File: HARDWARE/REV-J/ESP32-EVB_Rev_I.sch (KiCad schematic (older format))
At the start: 160 parts, among them CON1 TB3 DG306-5.0-3P, CON2 TB3 DG306-5.0-3P, Q1 BC817-40(SOT23), Q2 BC817-40(SOT23), Q3 Q12MHz/20pF/30ppm/2P/HC-49SM(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, Q4 BC817-40(SOT23), Q5 BC817-40(SOT23), Q6 BC817, Q7 BC817-40(SOT23), U1 BL4054B-42TPRN(SOT23-5), U10 BAT54C(SOT23-3), U2 SY8089AAAC(SOT23-5), U3 ESP-WROOM-32, U4 LAN8710A-EZC(QFN32), U5 CH340T(SSOP20W), U6 MCP2562-E/SN(SOIC-8_150mil), U7 RPM7236-H8, U8 NCP303LSN27T1G(SOT-23-5), U9 BAT54C(SOT23-3)

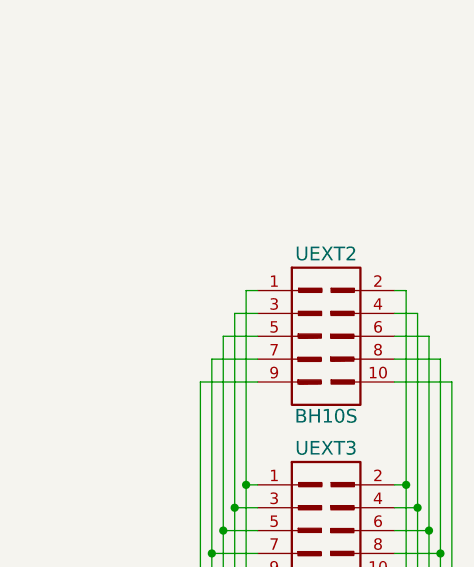
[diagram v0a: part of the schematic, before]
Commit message: fix UEXT extention
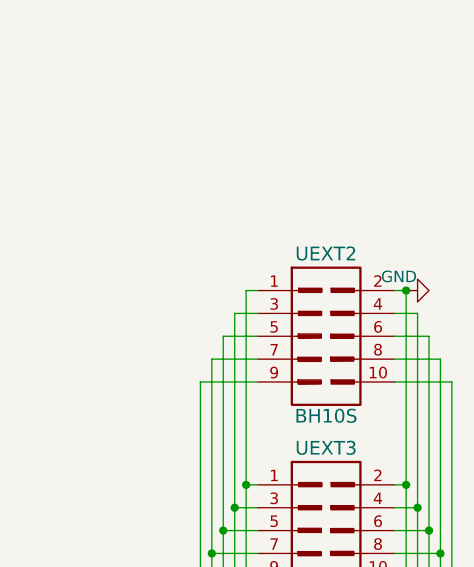
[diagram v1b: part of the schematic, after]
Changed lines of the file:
@@
 Wire Wire Line
 	23900 3950 23900 4750
+$Comp
+L ESP32-EVB_Rev_I:GND #PWR0118
+U 1 1 6378C996
+P 24800 2700
+F 0 "#PWR0118" H 24800 2450 50  0001 C CNN
+F 1 "GND" V 24860 2810 50  0000 R CNN
+F 2 "" H 24800 2700 60  0000 C CNN
+F 3 "" H 24800 2700 60  0000 C CNN
+	1    24800 2700
+	0    -1   -1   0
+$EndComp
+Connection ~ 24800 2700
 $EndSCHEMATC

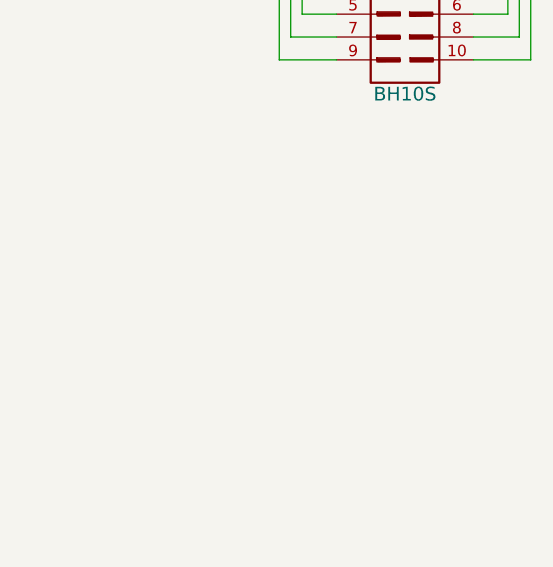
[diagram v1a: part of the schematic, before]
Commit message: add hole mount splitter
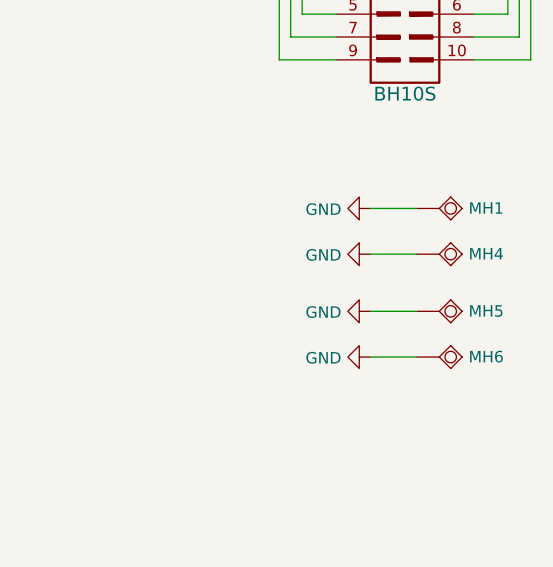
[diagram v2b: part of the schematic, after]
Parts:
- added MH1, MH4, MH5, MH6: Mounting_hole_Shield_3.3mm, MountingHole:MountingHole_3.2mm_M3_Pad_Via, symbol ESP32-EVB_Rev_I:Mounting_hole_Shield_3.3mm
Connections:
- wire segments 790 -> 794
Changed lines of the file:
@@
 $EndComp
 Connection ~ 24800 2700
+$Comp
+L ESP32-EVB_Rev_I:Mounting_hole_Shield_3.3mm MH1
+U 1 1 61522996
+P 24600 7000
+F 0 "MH1" H 24728 7000 50  0000 L CNN
+F 1 "Mounting_hole_Shield_3.3mm" H 24500 6885 50  0001 L BNN
+F 2 "MountingHole:MountingHole_3.2mm_M3_Pad_Via" H 24360 6925 20  0001 C CNN
+F 3 "" V 24600 7000 60  0000 C CNN
+F 4 "Value 1" H 24728 6954 60  0001 L CNN "Fieldname 1"
+F 5 "Value2" H 24600 7000 60  0001 C CNN "Fieldname2"
+F 6 "Value3" H 24600 7000 60  0001 C CNN "Fieldname3"
+	1    24600 7000
+	1    0    0    -1
+$EndComp
+$Comp
+L ESP32-EVB_Rev_I:GND #PWR0119
+U 1 1 6152299C
+P 24300 7000
+F 0 "#PWR0119" H 24300 6750 50  0001 C CNN
+F 1 "GND" V 24305 6872 50  0000 R CNN
+F 2 "" H 24300 7000 60  0000 C CNN
+F 3 "" H 24300 7000 60  0000 C CNN
+	1    24300 7000
+	0    1    1    0
+$EndComp
+Wire Wire Line
+	24300 7000 24500 7000
+$Comp
+L ESP32-EVB_Rev_I:Mounting_hole_Shield_3.3mm MH4
+U 1 1 615D4050
+P 24600 7200
+F 0 "MH4" H 24728 7200 50  0000 L CNN
+F 1 "Mounting_hole_Shield_3.3mm" H 24500 7085 50  0001 L BNN
+F 2 "MountingHole:MountingHole_3.2mm_M3_Pad_Via" H 24360 7125 20  0001 C CNN
+F 3 "" V 24600 7200 60  0000 C CNN
+F 4 "Value 1" H 24728 7154 60  0001 L CNN "Fieldname 1"
+F 5 "Value2" H 24600 7200 60  0001 C CNN "Fieldname2"
+F 6 "Value3" H 24600 7200 60  0001 C CNN "Fieldname3"
+	1    24600 7200
+	1    0    0    -1
+$EndComp
+$Comp
+L ESP32-EVB_Rev_I:GND #PWR0120
+U 1 1 615D4056
+P 24300 7200
+F 0 "#PWR0120" H 24300 6950 50  0001 C CNN
+F 1 "GND" V 24305 7072 50  0000 R CNN
+F 2 "" H 24300 7200 60  0000 C CNN
+F 3 "" H 24300 7200 60  0000 C CNN
+	1    24300 7200
+	0    1    1    0
+$EndComp
+Wire Wire Line
+	24300 7200 24500 7200
+$Comp
+L ESP32-EVB_Rev_I:Mounting_hole_Shield_3.3mm MH5
+U 1 1 61685A76
+P 24600 7450
+F 0 "MH5" H 24728 7450 50  0000 L CNN
+F 1 "Mounting_hole_Shield_3.3mm" H 24500 7335 50  0001 L BNN
+F 2 "MountingHole:MountingHole_3.2mm_M3_Pad_Via" H 24360 7375 20  0001 C CNN
+F 3 "" V 24600 7450 60  0000 C CNN
+F 4 "Value 1" H 24728 7404 60  0001 L CNN "Fieldname 1"
+F 5 "Value2" H 24600 7450 60  0001 C CNN "Fieldname2"
+F 6 "Value3" H 24600 7450 60  0001 C CNN "Fieldname3"
+	1    24600 7450
+	1    0    0    -1
+$EndComp
+$Comp
+L ESP32-EVB_Rev_I:GND #PWR0121
+U 1 1 61685A7C
+P 24300 7450
+F 0 "#PWR0121" H 24300 7200 50  0001 C CNN
+F 1 "GND" V 24305 7322 50  0000 R CNN
+F 2 "" H 24300 7450 60  0000 C CNN
+F 3 "" H 24300 7450 60  0000 C CNN
+	1    24300 7450
+	0    1    1    0
+$EndComp
+Wire Wire Line
+	24300 7450 24500 7450
+$Comp
+L ESP32-EVB_Rev_I:Mounting_hole_Shield_3.3mm MH6
+U 1 1 6173816D
+P 24600 7650
+F 0 "MH6" H 24728 7650 50  0000 L CNN
+F 1 "Mounting_hole_Shield_3.3mm" H 24500 7535 50  0001 L BNN
+F 2 "MountingHole:MountingHole_3.2mm_M3_Pad_Via" H 24360 7575 20  0001 C CNN
+F 3 "" V 24600 7650 60  0000 C CNN
+F 4 "Value 1" H 24728 7604 60  0001 L CNN "Fieldname 1"
+F 5 "Value2" H 24600 7650 60  0001 C CNN "Fieldname2"
+F 6 "Value3" H 24600 7650 60  0001 C CNN "Fieldname3"
+	1    24600 7650
+	1    0    0    -1
+$EndComp
+$Comp
+L ESP32-EVB_Rev_I:GND #PWR0122
+U 1 1 61738173
+P 24300 7650
+F 0 "#PWR0122" H 24300 7400 50  0001 C CNN
+F 1 "GND" V 24305 7522 50  0000 R CNN
+F 2 "" H 24300 7650 60  0000 C CNN
+F 3 "" H 24300 7650 60  0000 C CNN
+	1    24300 7650
+	0    1    1    0
+$EndComp
+Wire Wire Line
+	24300 7650 24500 7650
 $EndSCHEMATC
